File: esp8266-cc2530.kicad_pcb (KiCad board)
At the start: 2 copper layers, 43.7 x 43 mm, 36 parts, among them J1 CC2530_programmingHeader, J2 Conn_Coaxial, J3 USB_A, U1 WeMos_D1_mini, U2 AMS1117-3.3, U3 CC2530Fxxx, U4 RFX2401C, Y1 32.768kHz, Y2 32MHz

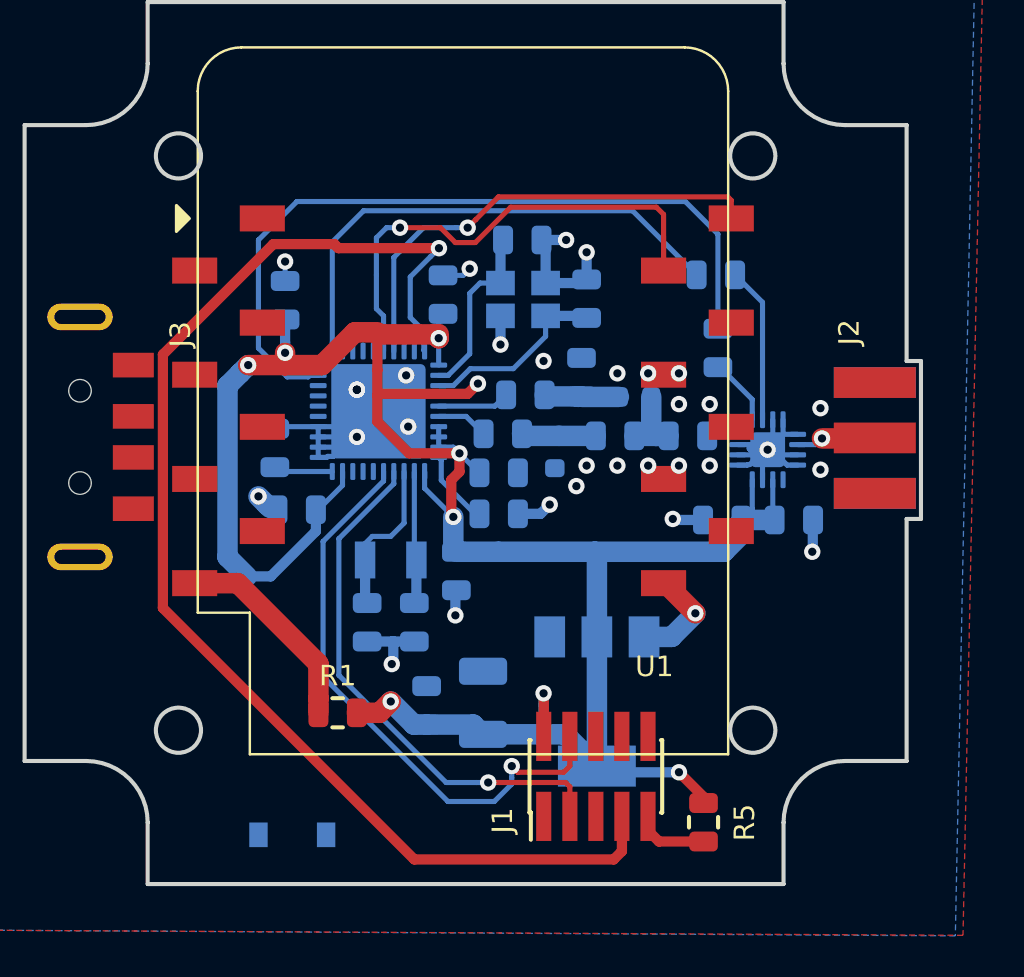
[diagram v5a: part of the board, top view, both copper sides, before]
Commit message: usb connector routed out
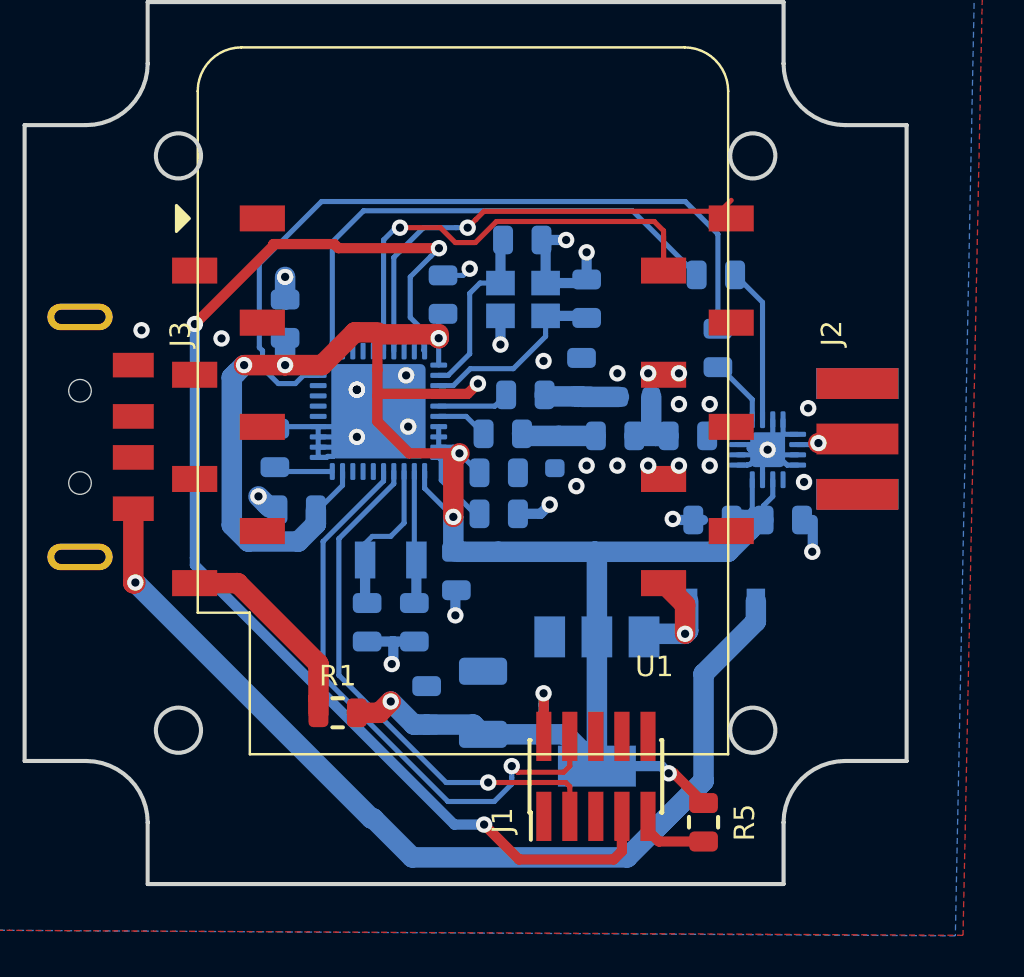
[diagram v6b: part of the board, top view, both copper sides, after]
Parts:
- moved D1 23.9 mm to (94.8, 49.1), turned to 0 degrees
- moved C3 0.90 mm to (73.5, 35.4)
- moved J2 0.85 mm to (101.5, 41.2)
- moved C20 0.54 mm to (97.8, 45.2)
- moved C19 0.47 mm to (94.4, 45.2)
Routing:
- net Net-(D1-Pad2): track 0.00 -> 51.7 mm, vias 0 -> 1
- net /~RST: track 63.3 -> 59.9 mm, vias 1 -> 3
- net VCC: track 119.8 -> 116.7 mm
- net Net-(J2-Pad1): track 5.34 -> 3.45 mm
- net /ESP_RX: track 25.5 -> 23.9 mm
- net Net-(D1-Pad1): track 5.14 -> 6.71 mm
- net /ESP_TX: track 23.2 -> 22.2 mm
- net GND: track 60.2 -> 60.5 mm, vias 29 -> 33
- net (no net): vias 2 -> 0
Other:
- board size 43.7 x 43 mm -> 43 x 43 mm

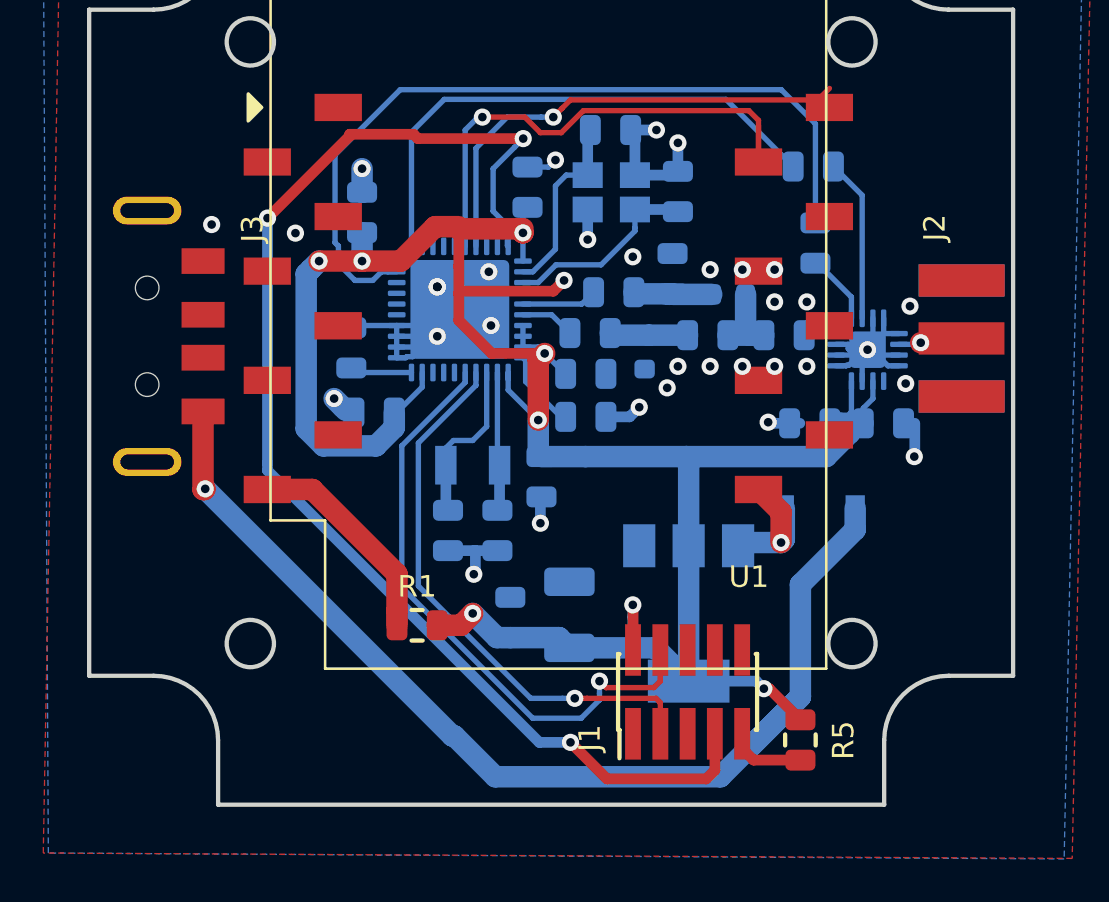
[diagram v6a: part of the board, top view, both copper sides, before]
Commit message: updated design rules
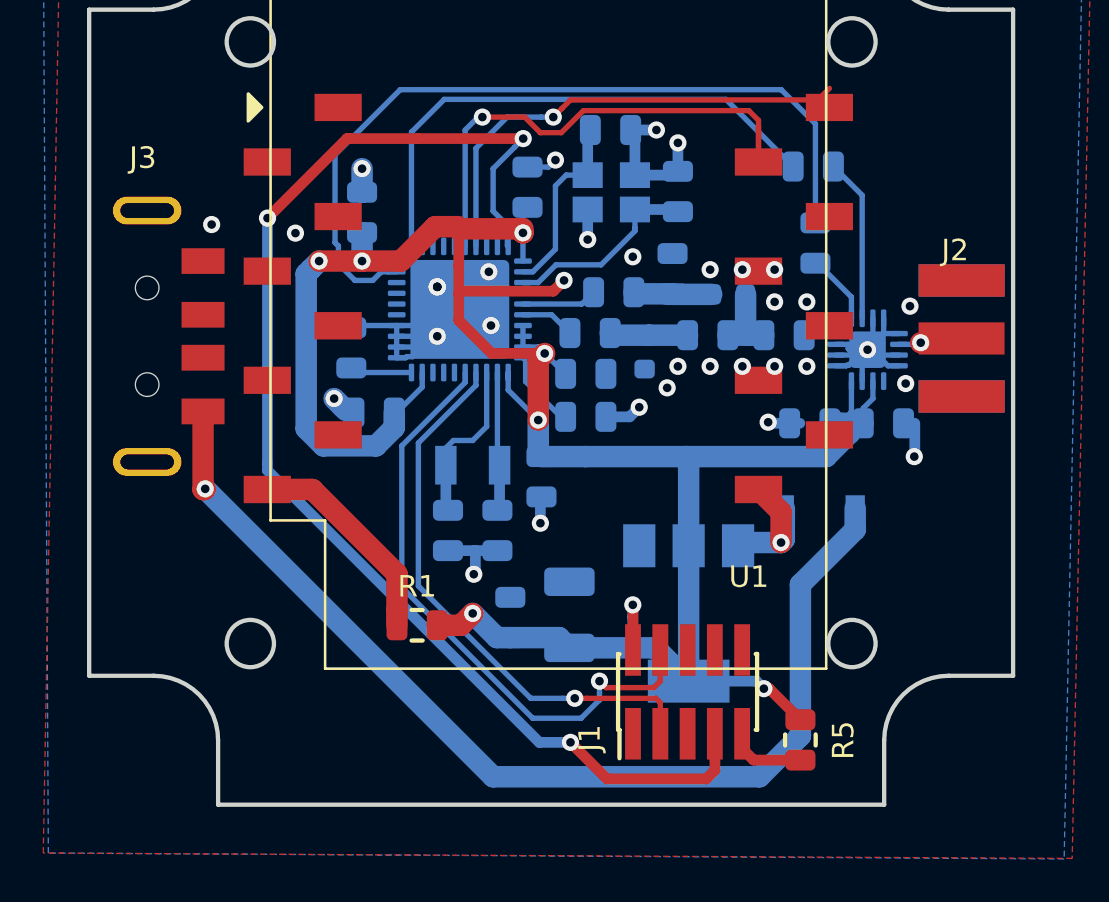
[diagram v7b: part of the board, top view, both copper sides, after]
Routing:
- net Net-(D1-Pad2): track 51.7 -> 49.4 mm
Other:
- board text added: "5/2020"
- board text added: "RevA"
- board text added: "WNG"
